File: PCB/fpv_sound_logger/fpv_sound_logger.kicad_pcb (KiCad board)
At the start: 2 copper layers, 29.5 x 21.4 mm, 45 parts, among them CN1 SM04B-SRSS-TB(LF)(SN), IC1 W25Q128JVSIQ, J2 MSD-4-A, U2 INMP441ACEZ-R7, U3 TLV75533PDBVR, U4 SC0914_13_, Y1 ABM8-272-T3

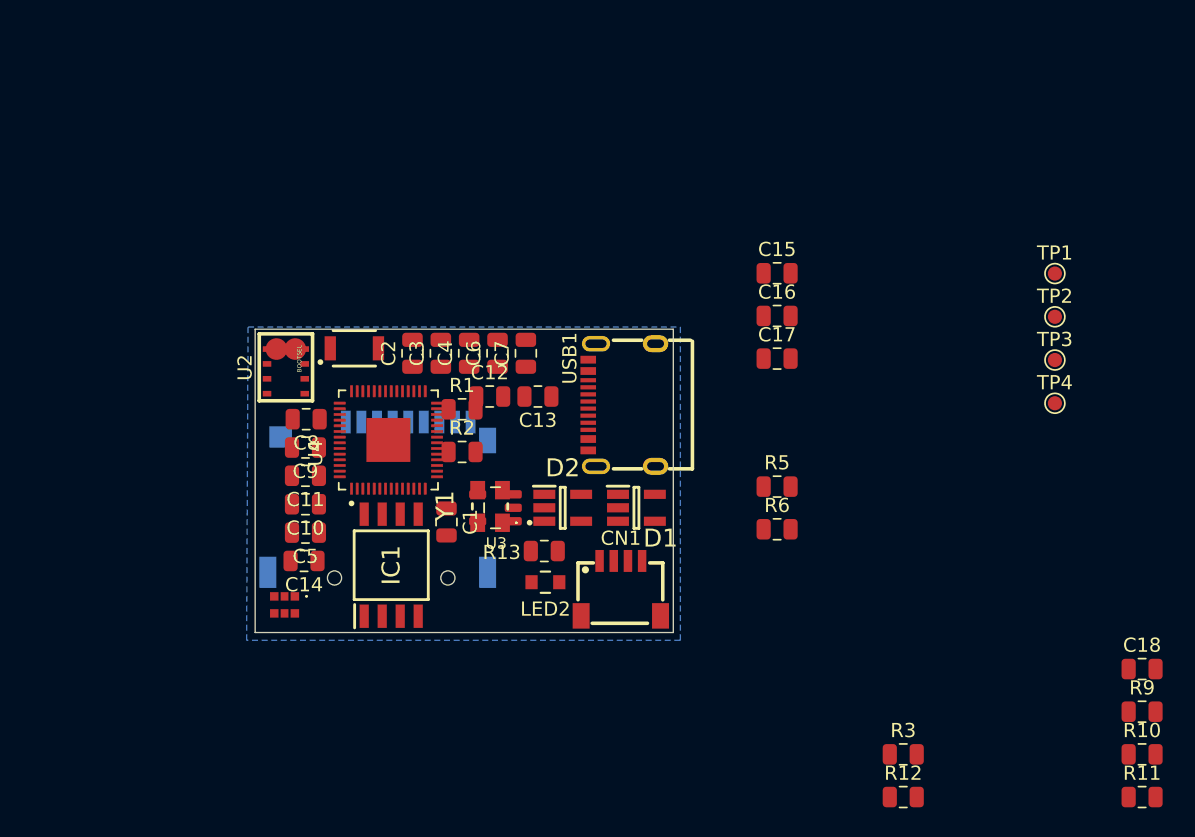
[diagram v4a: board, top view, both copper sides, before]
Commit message: place new components and started routing for v2
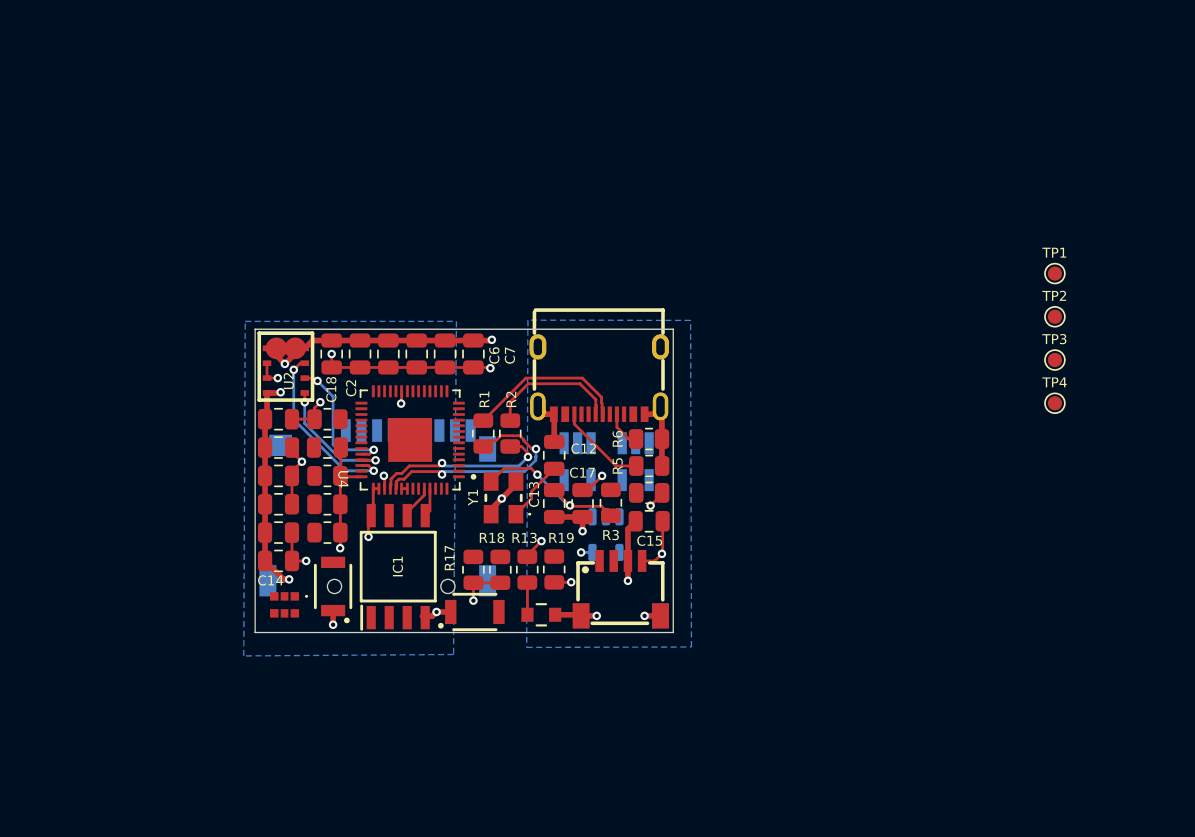
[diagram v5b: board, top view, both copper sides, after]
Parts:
- removed C16: 10u, Capacitor_SMD:C_0805_2012Metric
- added R17: 10k, Resistor_SMD:R_0805_2012Metric, F.Cu at (139.9, 97.0)
- added R18: 10k, Resistor_SMD:R_0805_2012Metric, F.Cu at (141.8, 97.0)
- added R19: 10k, Resistor_SMD:R_0805_2012Metric, F.Cu at (145.6, 97.0)
- added R20: 10k, Resistor_SMD:R_0805_2012Metric, F.Cu at (152.3, 91.6)
- added S2: B3U-1000P, fpv_sound_logger:B3U-1000P, F.Cu at (130.0, 98.2)
- D1, D2, U3: moved to B.Cu
- R1, R2: value 27.4 -> 27; footprint Capacitor_SMD:C_0805_2012Metric -> Resistor_SMD:R_0805_2012Metric
- R10, R11, R12, R13, R3, R5, R6, R9: footprint Capacitor_SMD:C_0805_2012Metric -> Resistor_SMD:R_0805_2012Metric
- moved R11 61.8 mm to (129.6, 90.4)
- moved C18 61.3 mm to (129.9, 81.8), turned to 90 degrees
- moved R10 60.1 mm to (129.6, 92.4)
- moved R9 58.8 mm to (129.6, 94.4)
- moved R12 48.6 mm to (129.6, 86.4)
- moved R3 27.2 mm to (149.6, 92.3), turned to 90 degrees
- moved S1 20.5 mm to (140.0, 100.0)
- moved C15 19.7 mm to (152.3, 93.6), turned to 180 degrees
- moved C17 17.1 mm to (147.6, 92.3), turned to -90 degrees
- moved R6 11.1 mm to (152.3, 87.8)
- moved C1 9.91 mm to (129.6, 88.4), turned to 180 degrees
- moved R5 9.14 mm to (152.3, 89.7)
- moved U3 8.02 mm to (149.2, 94.5), turned to -90 degrees
- moved C13 7.64 mm to (145.6, 92.3), turned to -90 degrees
- moved C12 6.16 mm to (145.6, 89.0), turned to 90 degrees
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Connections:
- net /MCU/RUN renamed RUN
- C15 pad 1: +3V3 -> +5V
- J2 pad 2: GPIO22 -> GPIO13
- J2 pad 3: GPIO18 -> GPIO11
- J2 pad 4: unconnected-(J2-VDD-Pad4) -> +3V3
- J2 pad 5: GPIO5 -> GPIO10
- J2 pad CD: unconnected-(J2-PadCD) -> GPIO14
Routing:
- net GND: track 0.00 -> 61.6 mm, vias 0 -> 11
- net +3V3: track 0.00 -> 41.1 mm, vias 0 -> 12
- net /MCU/USB_DIFF+: track 0.00 -> 16.4 mm, vias 0 -> 2
- net /MCU/USB_DIFF-: track 0.00 -> 12.9 mm, vias 0 -> 2
- net GPIO28_ADC2: track 0.00 -> 12.6 mm, vias 0 -> 2
- net Net-(Y1-CRYSTAL_2): track 0.00 -> 11.8 mm, vias 0 -> 2
- net USB_D+: track 0.00 -> 11.4 mm
- net GPIO26_ADC0: track 0.00 -> 9.95 mm, vias 0 -> 2
- net USB_D-: track 0.00 -> 9.43 mm
- net GPIO27_ADC1: track 0.00 -> 9.24 mm, vias 0 -> 2
- net +1V1: track 0.00 -> 6.39 mm, vias 0 -> 3
- net Net-(USB1-CC2): track 0.00 -> 6.28 mm
- net +5V: track 0.00 -> 5.44 mm, vias 0 -> 2
- net /MCU/XIN: track 0.00 -> 4.32 mm
- net /MCU/QSPI_SCLK: track 0.00 -> 2.90 mm
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- added copper zone on B.Cu, net +1V1
- added copper zone on In2.Cu, net +3V3
- added copper zone on B.Cu, net +5V
- added copper zone on In1.Cu, net GND
- removed copper zone on B.Cu, net GND
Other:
- copper layers 2 -> 4
- board text removed: "BOOTSEL"

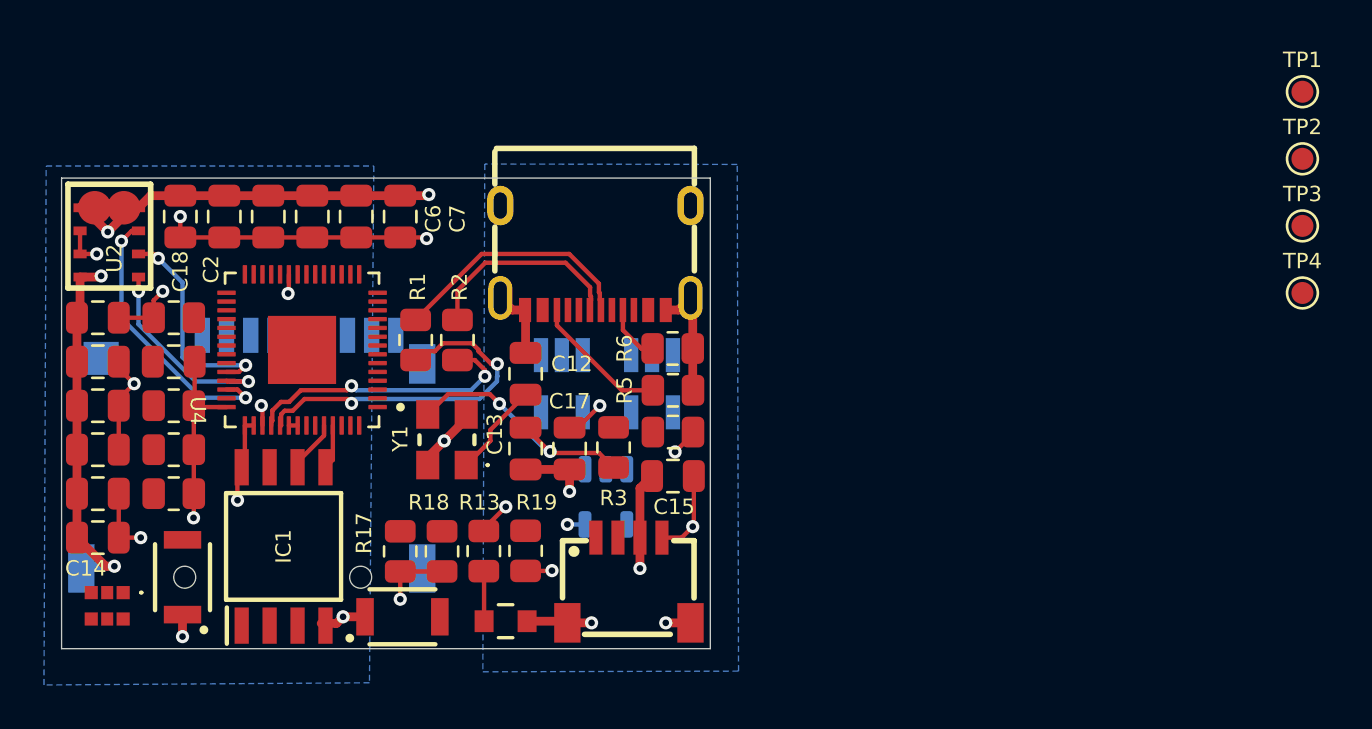
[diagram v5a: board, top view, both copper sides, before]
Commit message: Update component footprints and add manufacturer details in sensor schematic
- Changed resistor footprint from R_0805 to R_0603 for multiple components.
- Updated manufacturer part numbers, manufacturers, suppliers, and supplier parts for various components.
- Added manufacturer and supplier information for OMRON components.
- Removed outdated datasheet link and replaced with relevant part numbers for clarity.
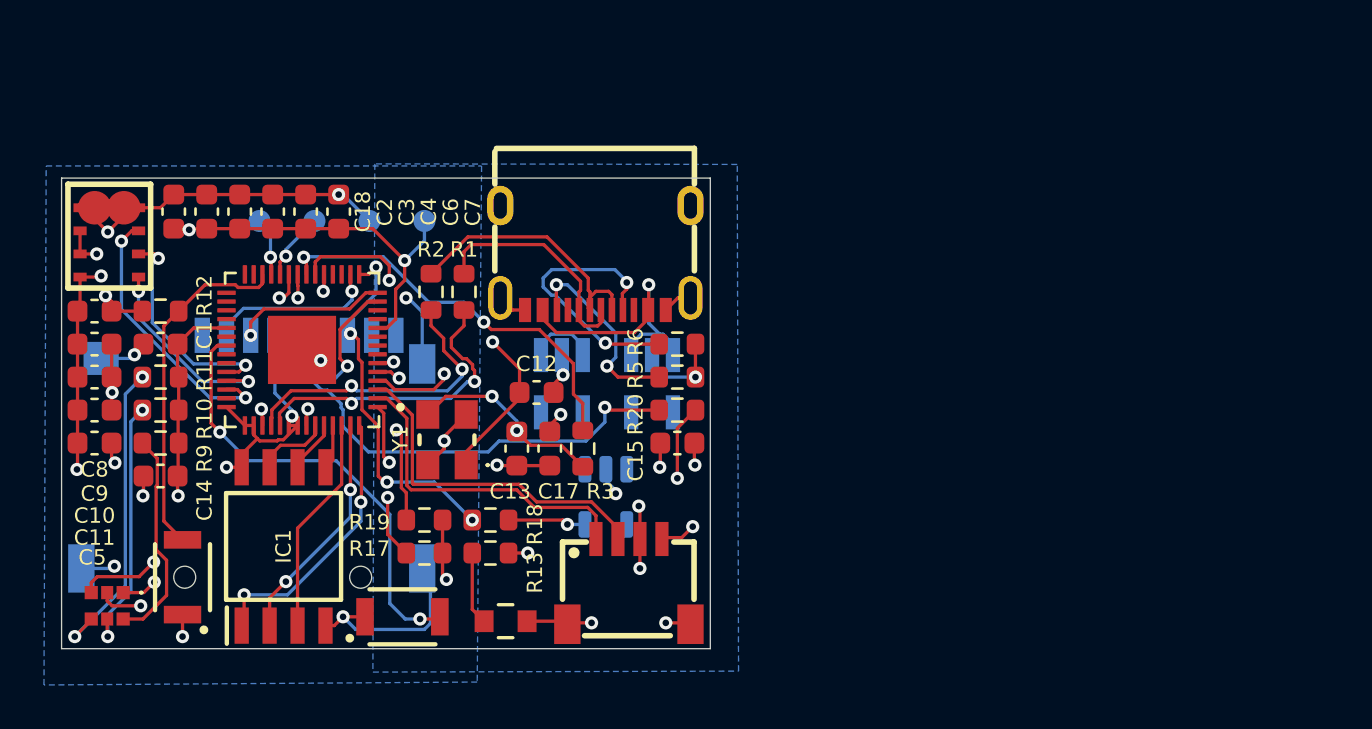
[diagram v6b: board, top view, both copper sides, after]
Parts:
- 3V3: renamed from TP4; moved to B.Cu
- C1, C10, C11, C12, C13, C14, C15, C17, C18, C2, C3, C4, C5, C6, C7, C8, C9: footprint Capacitor_SMD:C_0805_2012Metric -> Capacitor_SMD:C_0603_1608Metric
- CLK: renamed from TP1; moved to B.Cu
- DIO: renamed from TP2; moved to B.Cu
- GND: renamed from TP3; moved to B.Cu
- R1, R10, R11, R12, R13, R17, R18, R19, R2, R20, R3, R5, R6, R9: footprint Resistor_SMD:R_0805_2012Metric -> Resistor_SMD:R_0603_1608Metric
- moved DIO 47.5 mm to (133.5, 82.0), turned to 180 degrees
- moved CLK 45.3 mm to (136.0, 82.0), turned to 180 degrees
- moved GND 42.4 mm to (138.5, 82.0), turned to 180 degrees
- moved 3V3 40.1 mm to (141.0, 82.0), turned to 180 degrees
- moved R19 4.81 mm to (141.0, 95.6), turned to 180 degrees
- moved C14 4.00 mm to (129.0, 93.6)
- moved C10 3.30 mm to (126.0, 89.1)
- moved R1 3.10 mm to (142.8, 85.2)
- moved C7 2.81 mm to (137.1, 81.6)
- moved R18 2.62 mm to (144.0, 95.6), turned to 180 degrees
- moved R2 2.50 mm to (141.3, 85.2)
- moved R9 2.38 mm to (129.0, 92.1)
- moved C6 2.31 mm to (135.6, 81.6)
- moved C5 2.30 mm to (126.0, 92.1)
- moved R10 1.90 mm to (129.0, 90.6)
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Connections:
- net Net-(Y1-CRYSTAL_2) renamed /MCU/XOUT_RC
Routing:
- net GPIO10: track 0.00 -> 27.3 mm, vias 0 -> 2
- net GPIO2: track 0.00 -> 25.7 mm, vias 0 -> 2
- net GPIO4: track 0.00 -> 20.6 mm, vias 0 -> 2
- net GPIO23: track 0.00 -> 20.6 mm, vias 0 -> 2
- net GPIO11: track 0.00 -> 19.8 mm, vias 0 -> 2
- net GPIO3: track 0.00 -> 19.5 mm, vias 0 -> 2
- net GPIO13: track 0.00 -> 19.3 mm, vias 0 -> 2
- net /MCU/XOUT: track 0.00 -> 18.4 mm, vias 0 -> 2
- net GPIO12: track 0.00 -> 16.9 mm, vias 0 -> 4
- net +3V3: track 41.1 -> 57.8 mm, vias 12 -> 14
- net RUN: track 0.00 -> 15.9 mm
- net GPIO1/RX: track 0.00 -> 15.8 mm
- net GPIO0/TX: track 0.00 -> 14.9 mm
- net /sensor/GREEN: track 0.00 -> 14.2 mm, vias 0 -> 2
- net /MCU/XIN: track 4.32 -> 17.8 mm, vias 0 -> 2
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
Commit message: Refactor code structure for improved readability and maintainability
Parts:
- removed 3V3, CLK, DIO, GND: TestPoint, TestPoint:TestPoint_Pad_D1.0mm
- removed C18: 100n, Capacitor_SMD:C_0603_1608Metric
- removed U2: INMP441ACEZ-R7, fpv_sound_logger:MID-SMD_L4.7-W3.8_INMP441ACEZ
- added C19: 1u, Capacitor_SMD:C_0603_1608Metric, F.Cu at (131.1, 81.7)
- added MIC1: ~, fpv_sound_logger:MIC-TH_BD6.0-P1.90-D0.4-L-FD_GMI6050P-2CXXDB, F.Cu at (127.0, 82.0)
- added R14: 2k2, Resistor_SMD:R_0603_1608Metric, F.Cu at (132.6, 81.7)
- added TP1: TestPoint, TestPoint:TestPoint_Pad_D1.0mm, B.Cu at (135.2, 81.7)
- added TP2: TestPoint, TestPoint:TestPoint_Pad_D1.0mm, B.Cu at (133.0, 81.7)
- added TP3: TestPoint, TestPoint:TestPoint_Pad_D1.0mm, B.Cu at (137.5, 81.8)
- added TP4: TestPoint, TestPoint:TestPoint_Pad_D1.0mm, B.Cu at (139.8, 81.8)
- moved C2 3.00 mm to (134.1, 81.7)
- moved C3 3.00 mm to (135.6, 81.7)
- moved C4 3.00 mm to (137.1, 81.7)
- moved C6 3.00 mm to (138.6, 81.7)
- moved C7 3.00 mm to (140.1, 81.7)
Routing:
- net GPIO28_ADC2: track 12.4 -> 0.00 mm, vias 2 -> 0
- net GND: track 69.3 -> 59.8 mm, vias 22 -> 20
- net GPIO27_ADC1: track 9.07 -> 0.00 mm, vias 2 -> 0
- net +3V3: track 57.8 -> 51.8 mm, vias 14 -> 12
- net Net-(MIC1--): track 0.00 -> 5.63 mm
- net GPIO26_ADC0: track 10.1 -> 8.50 mm
- net +5V: track 3.56 -> 4.49 mm, vias 3 -> 4
- net SWD: track 2.65 -> 3.16 mm
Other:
- board size 29.5 x 21.4 mm -> 29.5 x 22.2 mm
